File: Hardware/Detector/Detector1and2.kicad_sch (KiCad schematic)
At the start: 55 parts, among them U1 AS321, U2 MCP6477, U4 AS339MTR-G1

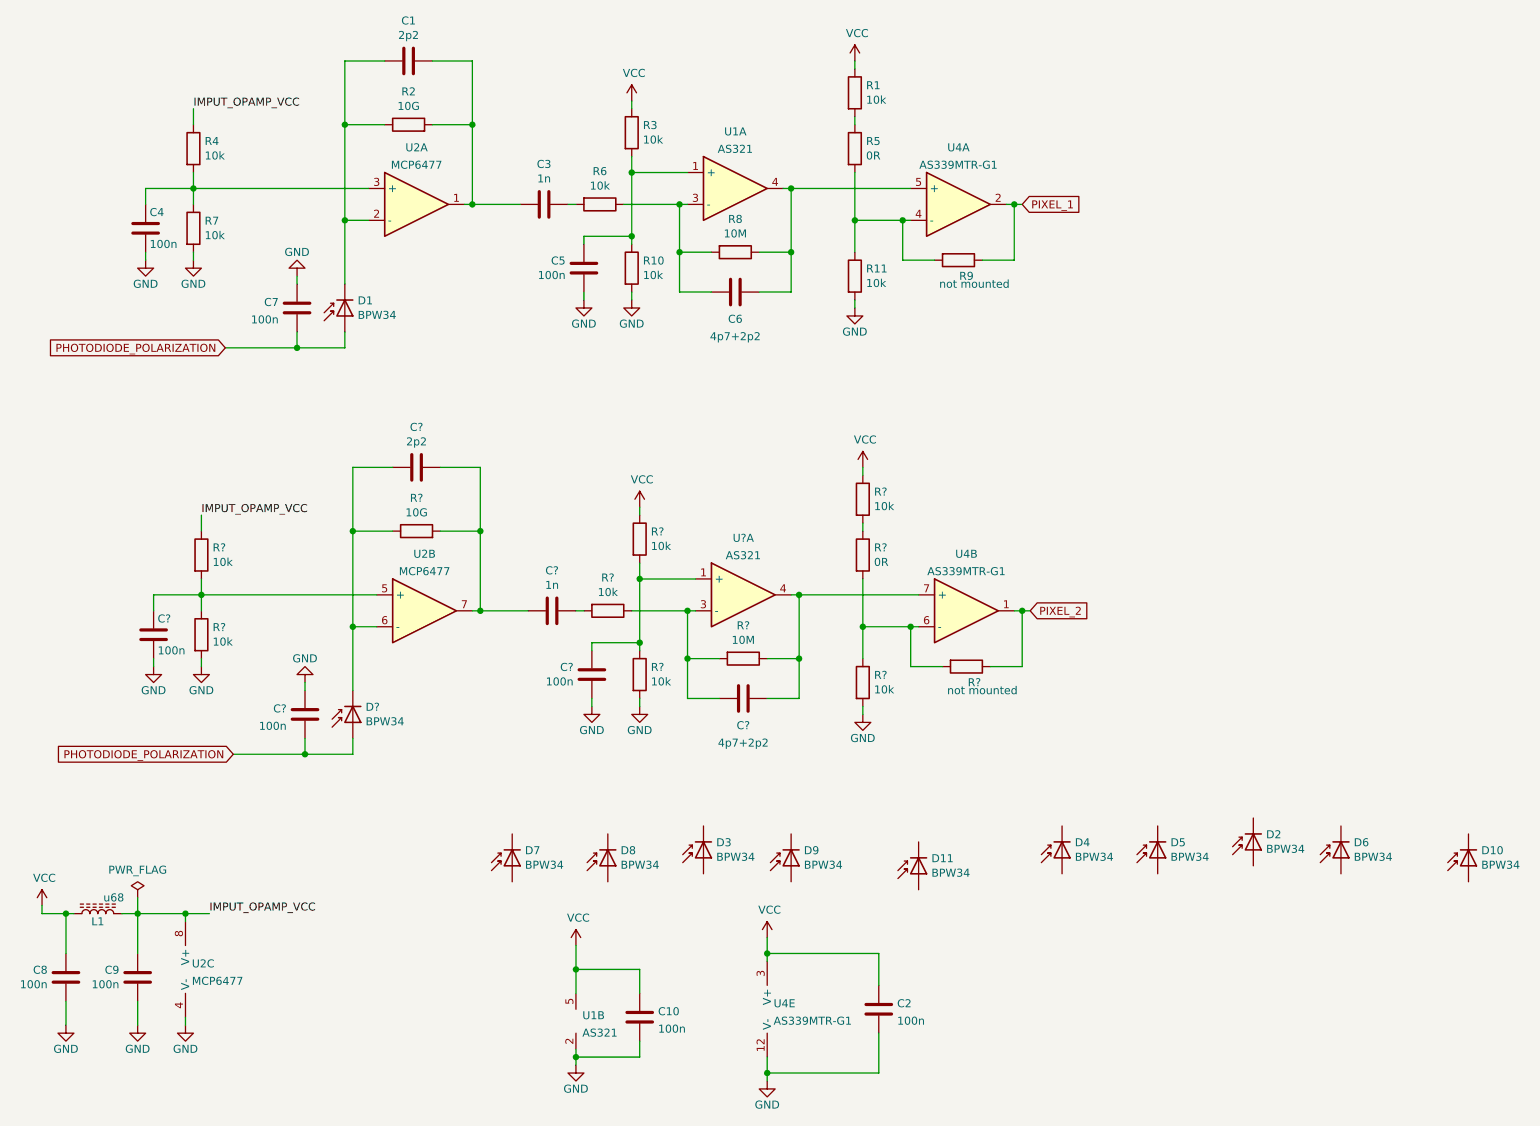
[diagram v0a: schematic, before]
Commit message: further implementation of low cost version
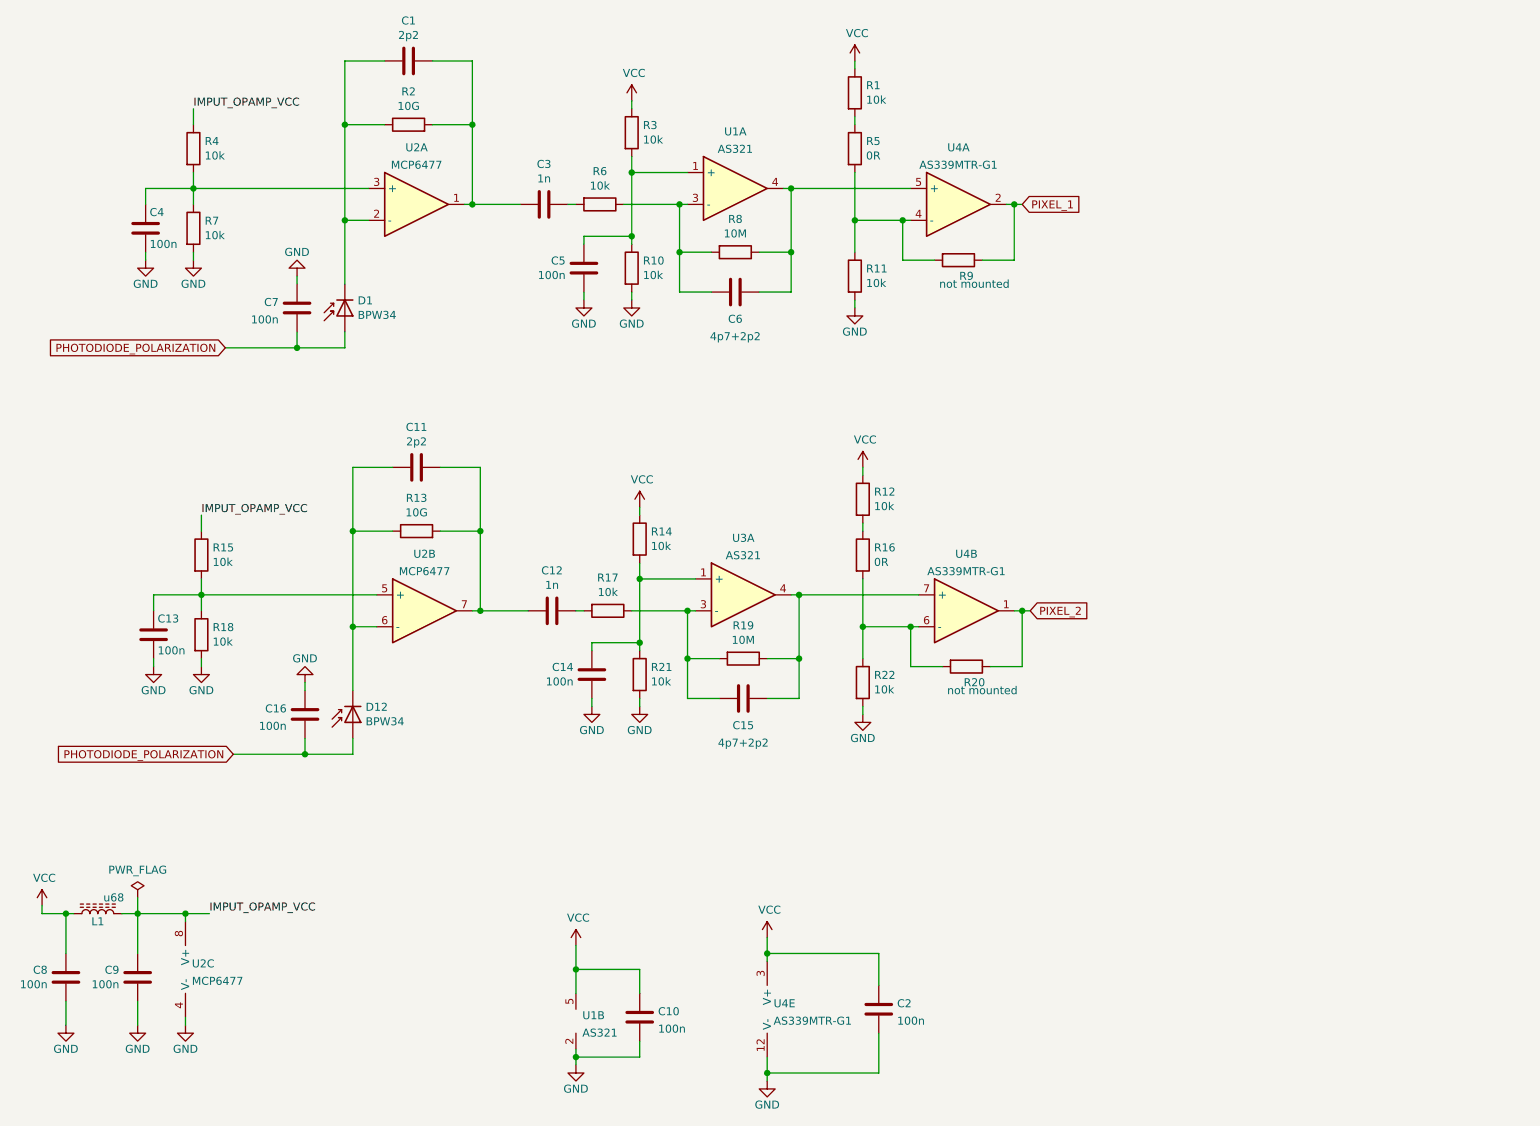
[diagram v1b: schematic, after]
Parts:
- removed D10, D11, D2, D3, D4, D5, D6, D7, D8, D9: BPW34, DiscretePixelDetectorForRadiationAnalysis:BPW 34 OSRAM, symbol Device:D_Photo
- gave numbers to parts that had none: 19

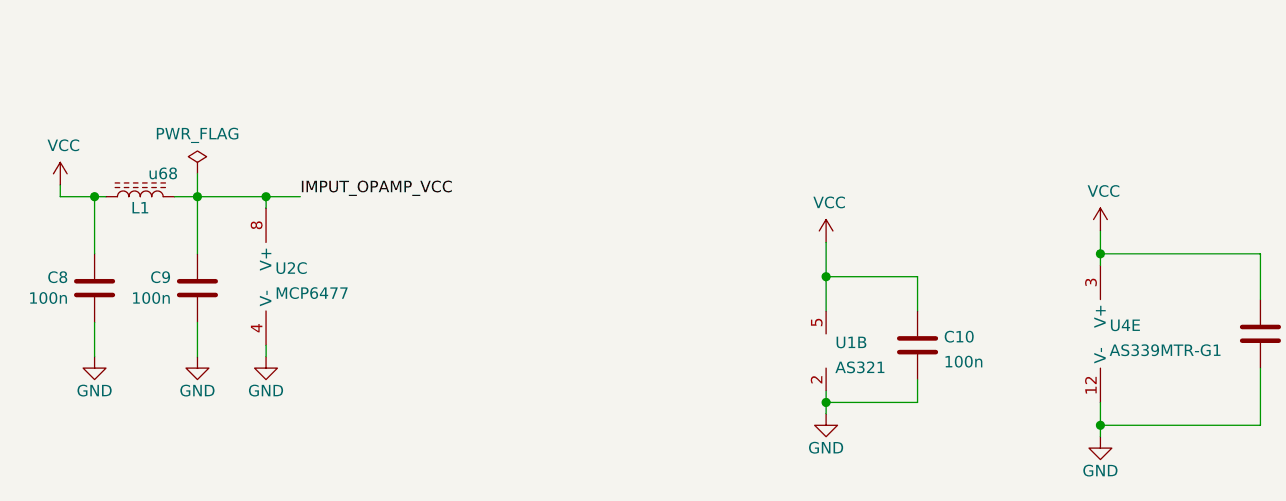
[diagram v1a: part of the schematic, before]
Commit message: fixed footprints, changed kicad scheet name, added a bit of decription to schematics
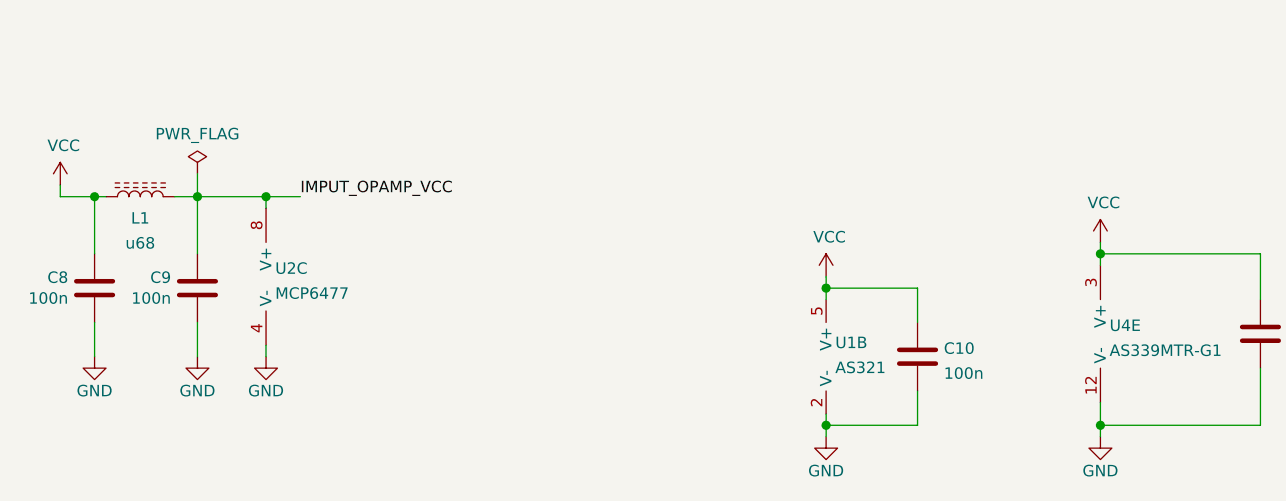
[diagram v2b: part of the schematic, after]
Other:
- moved on the sheet: C10
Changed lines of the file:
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@@
   (junction (at 101.6 99.06) (diameter 1.016) (color 0 0 0 0))
   (junction (at 101.6 111.76) (diameter 1.016) (color 0 0 0 0))
-  (junction (at 116.84 168.91) (diameter 1.016) (color 0 0 0 0))
-  (junction (at 116.84 182.88) (diameter 1.016) (color 0 0 0 0))
+  (junction (at 116.84 170.18) (diameter 1.016) (color 0 0 0 0))
+  (junction (at 116.84 185.42) (diameter 1.016) (color 0 0 0 0))
   (junction (at 125.73 41.91) (diameter 1.016) (color 0 0 0 0))
   (junction (at 125.73 52.07) (diameter 1.016) (color 0 0 0 0))
@@
     (stroke (width 0) (type solid) (color 0 0 0 0))
   )
-  (wire (pts (xy 116.84 165.1) (xy 116.84 168.91))
-    (stroke (width 0) (type solid) (color 0 0 0 0))
-  )
-  (wire (pts (xy 116.84 168.91) (xy 116.84 172.72))
-    (stroke (width 0) (type solid) (color 0 0 0 0))
-  )
-  (wire (pts (xy 116.84 168.91) (xy 127 168.91))
-    (stroke (width 0) (type solid) (color 0 0 0 0))
-  )
-  (wire (pts (xy 116.84 181.61) (xy 116.84 182.88))
-    (stroke (width 0) (type solid) (color 0 0 0 0))
-  )
-  (wire (pts (xy 116.84 182.88) (xy 116.84 184.15))
-    (stroke (width 0) (type solid) (color 0 0 0 0))
-  )
-  (wire (pts (xy 116.84 182.88) (xy 127 182.88))
+  (wire (pts (xy 116.84 168.91) (xy 116.84 170.18))
+    (stroke (width 0) (type solid) (color 0 0 0 0))
+  )
+  (wire (pts (xy 116.84 170.18) (xy 116.84 171.45))
+    (stroke (width 0) (type solid) (color 0 0 0 0))
+  )
+  (wire (pts (xy 116.84 170.18) (xy 127 170.18))
+    (stroke (width 0) (type solid) (color 0 0 0 0))
+  )
+  (wire (pts (xy 116.84 184.15) (xy 116.84 185.42))
+    (stroke (width 0) (type solid) (color 0 0 0 0))
+  )
+  (wire (pts (xy 116.84 185.42) (xy 116.84 186.69))
+    (stroke (width 0) (type solid) (color 0 0 0 0))
+  )
+  (wire (pts (xy 116.84 185.42) (xy 127 185.42))
     (stroke (width 0) (type solid) (color 0 0 0 0))
   )
@@
     (stroke (width 0) (type solid) (color 0 0 0 0))
   )
-  (wire (pts (xy 127 172.72) (xy 127 168.91))
-    (stroke (width 0) (type solid) (color 0 0 0 0))
-  )
-  (wire (pts (xy 127 182.88) (xy 127 180.34))
+  (wire (pts (xy 127 170.18) (xy 127 173.99))
+    (stroke (width 0) (type solid) (color 0 0 0 0))
+  )
+  (wire (pts (xy 127 181.61) (xy 127 185.42))
     (stroke (width 0) (type solid) (color 0 0 0 0))
   )
@@
     (stroke (width 0) (type solid) (color 0 0 0 0))
   )
-  (wire (pts (xy 147.32 163.83) (xy 147.32 166.37))
+  (wire (pts (xy 147.32 165.1) (xy 147.32 166.37))
     (stroke (width 0) (type solid) (color 0 0 0 0))
   )
@@
     (pin "1")
   )
-  (symbol (lib_id "power:VCC") (at 116.84 165.1 0) (unit 1)
-    (in_bom yes) (on_board yes)
-    (property "Reference" "#PWR015" (id 0) (at 116.84 168.91 0)
-      (effects (font (size 1.27 1.27)) hide)
-    )
-    (property "Value" "VCC" (id 1) (at 117.221 160.7058 0))
-    (property "Footprint" "" (id 2) (at 116.84 165.1 0)
-      (effects (font (size 1.27 1.27)) hide)
-    )
-    (property "Datasheet" "" (id 3) (at 116.84 165.1 0)
+  (symbol (lib_id "power:VCC") (at 116.84 168.91 0) (unit 1)
+    (in_bom yes) (on_board yes)
+    (property "Reference" "#PWR015" (id 0) (at 116.84 172.72 0)
+      (effects (font (size 1.27 1.27)) hide)
+    )
+    (property "Value" "VCC" (id 1) (at 117.221 164.5158 0))
+    (property "Footprint" "" (id 2) (at 116.84 168.91 0)
+      (effects (font (size 1.27 1.27)) hide)
+    )
+    (property "Datasheet" "" (id 3) (at 116.84 168.91 0)
       (effects (font (size 1.27 1.27)) hide)
     )
@@
     (pin "1")
   )
-  (symbol (lib_id "power:VCC") (at 147.32 163.83 0) (unit 1)
-    (in_bom yes) (on_board yes)
-    (property "Reference" "#PWR03" (id 0) (at 147.32 167.64 0)
-      (effects (font (size 1.27 1.27)) hide)
-    )
-    (property "Value" "VCC" (id 1) (at 147.701 159.4358 0))
-    (property "Footprint" "" (id 2) (at 147.32 163.83 0)
-      (effects (font (size 1.27 1.27)) hide)
-    )
-    (property "Datasheet" "" (id 3) (at 147.32 163.83 0)
+  (symbol (lib_id "power:VCC") (at 147.32 165.1 0) (unit 1)
+    (in_bom yes) (on_board yes)
+    (property "Reference" "#PWR03" (id 0) (at 147.32 168.91 0)
+      (effects (font (size 1.27 1.27)) hide)
+    )
+    (property "Value" "VCC" (id 1) (at 147.701 160.7058 0))
+    (property "Footprint" "" (id 2) (at 147.32 165.1 0)
+      (effects (font (size 1.27 1.27)) hide)
+    )
+    (property "Datasheet" "" (id 3) (at 147.32 165.1 0)
       (effects (font (size 1.27 1.27)) hide)
     )
@@
     (pin "1")
   )
-  (symbol (lib_id "DiscretePixelDetectorForRadiationAnalysis:AS321") (at 116.84 176.53 0) (unit 2)
-    (in_bom yes) (on_board yes) (fields_autoplaced)
-    (property "Reference" "U1" (id 0) (at 117.8561 176.2565 0)
-      (effects (font (size 1.27 1.27)) (justify left))
-    )
-    (property "Value" "AS321" (id 1) (at 117.8561 179.0316 0)
-      (effects (font (size 1.27 1.27)) (justify left))
-    )
-    (property "Footprint" "Package_TO_SOT_SMD:SOT-23-5" (id 2) (at 116.84 176.53 0)
-      (effects (font (size 1.27 1.27)) hide)
-    )
-    (property "Datasheet" "https://www.tme.eu/Document/ff04728045a484fb1c57ffb6d73e1bf1/AS321.pdf" (id 3) (at 116.84 176.53 0)
-      (effects (font (size 1.27 1.27)) hide)
-    )
-    (pin "2")
-    (pin "5")
-  )
   (symbol (lib_id "power:GND") (at 35.56 177.8 0) (mirror y) (unit 1)
     (in_bom yes) (on_board yes)
@@
     (pin "1")
   )
-  (symbol (lib_id "power:GND") (at 116.84 184.15 0) (unit 1)
-    (in_bom yes) (on_board yes)
-    (property "Reference" "#PWR019" (id 0) (at 116.84 190.5 0)
-      (effects (font (size 1.27 1.27)) hide)
-    )
-    (property "Value" "GND" (id 1) (at 116.84 187.96 0))
-    (property "Footprint" "" (id 2) (at 116.84 184.15 0)
-      (effects (font (size 1.27 1.27)) hide)
-    )
-    (property "Datasheet" "" (id 3) (at 116.84 184.15 0)
+  (symbol (lib_id "power:GND") (at 116.84 186.69 0) (unit 1)
+    (in_bom yes) (on_board yes)
+    (property "Reference" "#PWR019" (id 0) (at 116.84 193.04 0)
+      (effects (font (size 1.27 1.27)) hide)
+    )
+    (property "Value" "GND" (id 1) (at 116.84 190.5 0))
+    (property "Footprint" "" (id 2) (at 116.84 186.69 0)
+      (effects (font (size 1.27 1.27)) hide)
+    )
+    (property "Datasheet" "" (id 3) (at 116.84 186.69 0)
       (effects (font (size 1.27 1.27)) hide)
     )
@@
     )
     (pin "1")
+  )
+  (symbol (lib_id "DiscretePixelDetectorForRadiationAnalysis:AS321") (at 116.84 176.53 0) (unit 2)
+    (in_bom yes) (on_board yes)
+    (property "Reference" "U1" (id 0) (at 117.8561 176.2565 0)
+      (effects (font (size 1.27 1.27)) (justify left))
+    )
+    (property "Value" "AS321" (id 1) (at 117.8561 179.0316 0)
+      (effects (font (size 1.27 1.27)) (justify left))
+    )
+    (property "Footprint" "Package_TO_SOT_SMD:SOT-23-5" (id 2) (at 116.84 176.53 0)
+      (effects (font (size 1.27 1.27)) hide)
+    )
+    (property "Datasheet" "https://www.tme.eu/Document/ff04728045a484fb1c57ffb6d73e1bf1/AS321.pdf" (id 3) (at 116.84 176.53 0)
+      (effects (font (size 1.27 1.27)) hide)
+    )
+    (pin "2")
+    (pin "5")
   )
   (symbol (lib_id "Device:Opamp_Dual_Generic") (at 57.15 168.91 0) (unit 3)
@@
   )
   (symbol (lib_id "Device:L_Core_Ferrite") (at 40.64 160.02 270) (mirror x) (unit 1)
-    (in_bom yes) (on_board yes)
-    (property "Reference" "L1" (id 0) (at 40.64 161.29 90))
-    (property "Value" "u68" (id 1) (at 43.18 157.48 90))
+    (in_bom yes) (on_board yes) (fields_autoplaced)
+    (property "Reference" "L1" (id 0) (at 40.64 162.4236 90))
+    (property "Value" "u68" (id 1) (at 40.64 165.1987 90))
     (property "Footprint" "Inductor_SMD:L_0805_2012Metric" (id 2) (at 40.64 160.02 0)
       (effects (font (size 1.27 1.27)) hide)
@@
     (pin "2")
   )
-  (symbol (lib_id "Device:C") (at 127 176.53 0) (unit 1)
+  (symbol (lib_id "Device:C") (at 127 177.8 0) (unit 1)
     (in_bom yes) (on_board yes) (fields_autoplaced)
-    (property "Reference" "C10" (id 0) (at 129.9211 175.6215 0)
-      (effects (font (size 1.27 1.27)) (justify left))
-    )
-    (property "Value" "100n" (id 1) (at 129.9211 178.3966 0)
-      (effects (font (size 1.27 1.27)) (justify left))
-    )
-    (property "Footprint" "Capacitor_SMD:C_0402_1005Metric" (id 2) (at 127.9652 180.34 0)
-      (effects (font (size 1.27 1.27)) hide)
-    )
-    (property "Datasheet" "" (id 3) (at 127 176.53 0)
+    (property "Reference" "C10" (id 0) (at 129.9211 176.8915 0)
+      (effects (font (size 1.27 1.27)) (justify left))
+    )
+    (property "Value" "100n" (id 1) (at 129.9211 179.6666 0)
+      (effects (font (size 1.27 1.27)) (justify left))
+    )
+    (property "Footprint" "Capacitor_SMD:C_0402_1005Metric" (id 2) (at 127.9652 181.61 0)
+      (effects (font (size 1.27 1.27)) hide)
+    )
+    (property "Datasheet" "" (id 3) (at 127 177.8 0)
       (effects (font (size 1.27 1.27)) hide)
     )
@@
       (effects (font (size 1.27 1.27)) hide)
     )
-    (property "Datasheet" "" (id 3) (at 80.01 63.5 0)
-      (effects (font (size 1.27 1.27)) hide)
-    )
+    (property "Datasheet" "~" (id 3) (at 80.01 63.5 0)
+      (effects (font (size 1.27 1.27)) hide)
+    )
